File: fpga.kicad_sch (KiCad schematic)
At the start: 2 parts, among them Y1 CXO_DIP14

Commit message: add notes
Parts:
- added C10, C11, C12, C13, C14, C15, C16, C17, C18, C19, C20, C21: 0.1uF, Capacitor_SMD:C_0603_1608Metric, symbol Device:C_Small
- added R10, R11, R12, R13, R14, R15, R16, R17, R18, R19, R20, R21, R22, R23, R24, R25, R26, R27, R28, R29, R30, R31, R32, R33, R34, R7, R8, R9: 220R, Resistor_SMD:R_0603_1608Metric, symbol Device:R_Small
- added U3, U4, U7: TXU0104PWR, Library:TSSOP_0104PWR, symbol Library:TXU0104PWR
- added U5, U6, U8: TXB0104PWR, Library:TSSOP_0104PWR, symbol Library:TXB0104PWR
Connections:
- net +3.3V: now also Y1.1 (EN), Y1.14 (Vcc), C15.1, C16.1, C17.1, C18.1, C19.1, C20.1, U3.1 (VCCA), U4.1 (VCCA), U5.1 (VCCA), U6.1 (VCCA), U7.1 (VCCA), U8.7 (GND)
- net +5V: now also C10.1, C11.1, C12.1, C13.1, C14.1, C21.1, U3.14 (VCCB), U3.8 (OE), U4.14 (VCCB), U4.8 (OE), U5.14 (VCCB), U5.8 (OE), U6.14 (VCCB), U6.8 (OE), U7.14 (VCCB), U7.8 (OE), U8.14 (VCCB), U8.8 (OE); no longer Y1.1 (EN), Y1.14 (Vcc)
- net GND: now also C10.2, C11.2, C12.2, C13.2, C14.2, C15.2, C16.2, C17.2, C18.2, C19.2, C20.2, C21.2, U3.7 (GND), U4.7 (GND), U5.7 (GND), U6.7 (GND), U7.7 (GND), U8.1 (VCCA)
- net DL5: now reaches U2.10 (R7)
- net at U2.11 (R6): now also U7.3 (A2)
- net DL4: now reaches U2.12 (T5)
- net at U2.13 (R5): now also U7.2 (A1)
- net DL3: now reaches U2.14 (T4)
- net Z0: now reaches U2.15 (U6)
- net DL2: now reaches U2.16 (U5)
- net Z1: now reaches U2.17 (V4)
- net DL1: now reaches U2.18 (U4)
- net Z2: now reaches U2.19 (V3)
- net DL0: now reaches U2.20 (V2)
- net Z3: now reaches U2.21 (U2)
- net at U2.22 (U1): now also U4.3 (A2)
- net Z4: now reaches U2.23 (P4)
- net at U2.24 (T3): now also U4.4 (A3)
- net Z5: now reaches U2.25 (R3)
- net at U2.26 (T2): now also U4.5 (A4)
- net Z6: now reaches U2.27 (N4)
- net at U2.28 (P3): now also R7.1
- net Z7: now reaches U2.29 (M6)
- net at U2.30 (M5): now also R16.1
- net Z8: now reaches U2.31 (L5)
- net at U2.32 (L4): now also R15.1
- net Z9: now reaches U2.33 (K3)
- net at U2.34 (K5): now also R14.1
- net Z10: now reaches U2.35 (P1)
- net at U2.36 (R1): now also R8.1
- net Z11: now reaches U2.37 (N1)
- net at U2.38 (N2): now also R9.1
- net Z12: now reaches U2.39 (M2)
- net at U2.40 (M1): now also R10.1
- net Z13: now reaches U2.41 (J5)
- net at U2.42 (J4): now also R11.1
- net Z14: now reaches U2.43 (J6)
- net at U2.44 (K6): now also R12.1
- net Z15: now reaches U2.45 (L2)
- net at U2.46 (L3): now also R13.1
- net Z16: now reaches U2.47 (K2)
- net at U2.48 (K1): now also R34.1
- net at U2.5 (V8): now also U4.2 (A1)
- net DL7: now reaches U2.6 (V7)
- net at U2.7 (U7): now also U7.5 (A4)
- net DL6: now reaches U2.8 (V6)
- net at U2.9 (T7): now also U7.4 (A3)
- net at U2.55 (F18): now also U6.5 (A4)
- net at U2.56 (G17): now also U6.4 (A3)
- net at U2.57 (E18): now also U6.3 (A2)
- net at U2.58 (F17): now also U6.2 (A1)
- net at U2.59 (D18): now also U5.2 (A1)
- net at U2.60 (E17): now also U5.3 (A2)
- net at U2.61 (C17): now also U5.4 (A3)
- net at U2.62 (C18): now also U5.5 (A4)
- net at U2.63 (G15): now also R17.1
- net at U2.65 (F15): now also R18.1
- net at U2.67 (E16): now also R19.1
- net at U2.68 (E15): now also U3.2 (A1)
- net at U2.69 (D16): now also R20.1
- net at U2.70 (D15): now also U3.3 (A2)
- net at U2.71 (A17): now also R21.1
- net at U2.72 (B17): now also U3.4 (A3)
- net at U2.73 (C16): now also R22.1
- net at U2.74 (B16): now also U3.5 (A4)
- net at U2.75 (A15): now also R23.1
- net Z21: now reaches U2.76 (B15)
- net at U2.77 (A14): now also R24.1
- net Z20: now reaches U2.78 (B14)
- net at U2.79 (C14): now also R25.1
- net Z19: now reaches U2.80 (D14)
- net at U2.81 (C13): now also R26.1
- net Z18: now reaches U2.82 (D13)
- net at U2.83 (A13): now also R27.1
- net Z17: now reaches U2.84 (C12)
- net at U2.85 (F14): now also R28.1
- net at U2.86 (E13): now also R33.1
- net at U2.87 (B12): now also R29.1
- net at U2.88 (A12): now also U8.2 (A1)
- net at U2.89 (C11): now also R30.1
- net at U2.90 (B11): now also U8.3 (A2)
- net at U2.91 (D11): now also R31.1
- net at U2.93 (C9): now also R32.1
- new net A0: R17.2
- new net A1: R18.2
- new net A10: R27.2
- new net A11: R28.2
- new net A12: R29.2
- new net A13: R30.2
- new net A14: R31.2
- new net A15: R32.2
- new net A2: R19.2
- new net A3: R20.2
- new net A4: R21.2
- new net A5: R22.2
- new net A6: R23.2
- new net A7: R24.2
- new net A8: R25.2
- new net A9: R26.2
- new net AVMA: R15.2
- new net BA: R11.2
- new net BS: R13.2
- new net CPU_BUSY: R16.2
- new net D0: U5.10 (B4)
- new net D1: U5.11 (B3)
- new net D2: U5.12 (B2)
- new net D3: U5.13 (B1)
- new net D4: U6.10 (B4)
- new net D5: U6.11 (B3)
- new net D6: U6.12 (B2)
- new net D7: U6.13 (B1)
- new net E: U3.13 (B1Y)
- new net EXTMEN: R33.2
- new net LIC: R9.2
- new net Q: U3.12 (B2Y)
- new net R0: U8.12 (B2)
- new net R1: U8.13 (B1)
- new net R/~{W}: R34.2
- new net S0: U4.13 (B1Y)
- new net S1: U7.10 (B4Y)
- new net S2: U7.11 (B3Y)
- new net S3: U7.12 (B2Y)
- new net S4: U7.13 (B1Y)
- new net TSC: R14.2
- new net VCLK: U3.10 (B4Y)
- new net ~{FIRQ}: U4.11 (B3Y)
- new net ~{FIRQ}p: R10.2
- new net ~{HALT}: U3.11 (B3Y)
- new net ~{IRQ}: U4.12 (B2Y)
- new net ~{IRQ}p: R8.2
- new net ~{NMI}: U4.10 (B4Y)
- new net ~{NMI}p: R12.2
- new net ~{RESET}: R7.2
- no-connect marks 0 -> 24
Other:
- note added: "Crystal footprint needs to meet DIP14 and DIP8 specs"
- moved on the sheet: U2A, U2B, Y1

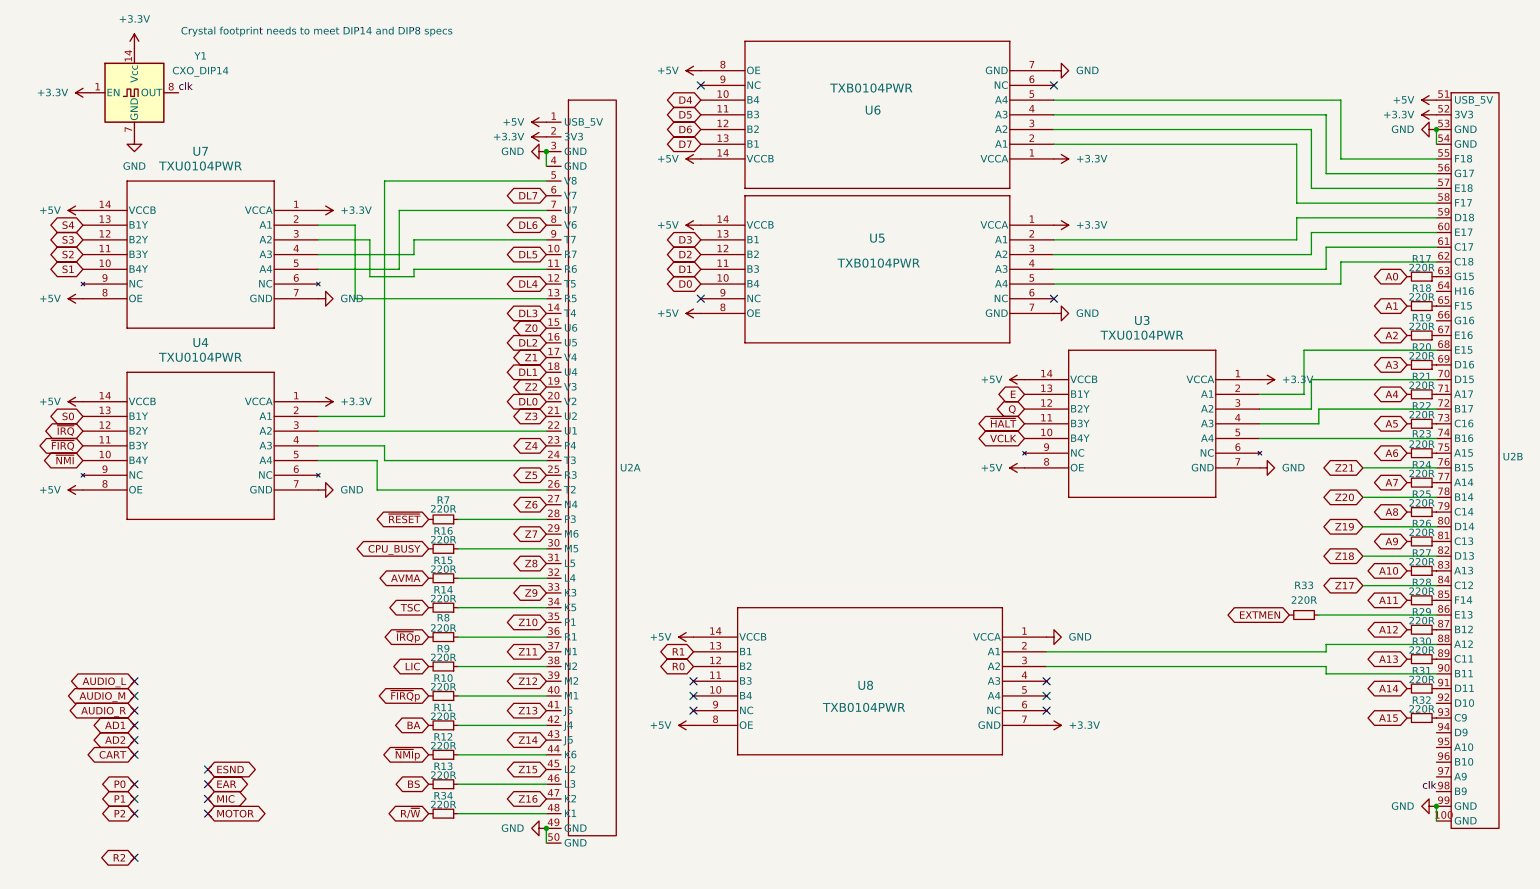
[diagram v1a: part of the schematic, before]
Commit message: revise bus tracing
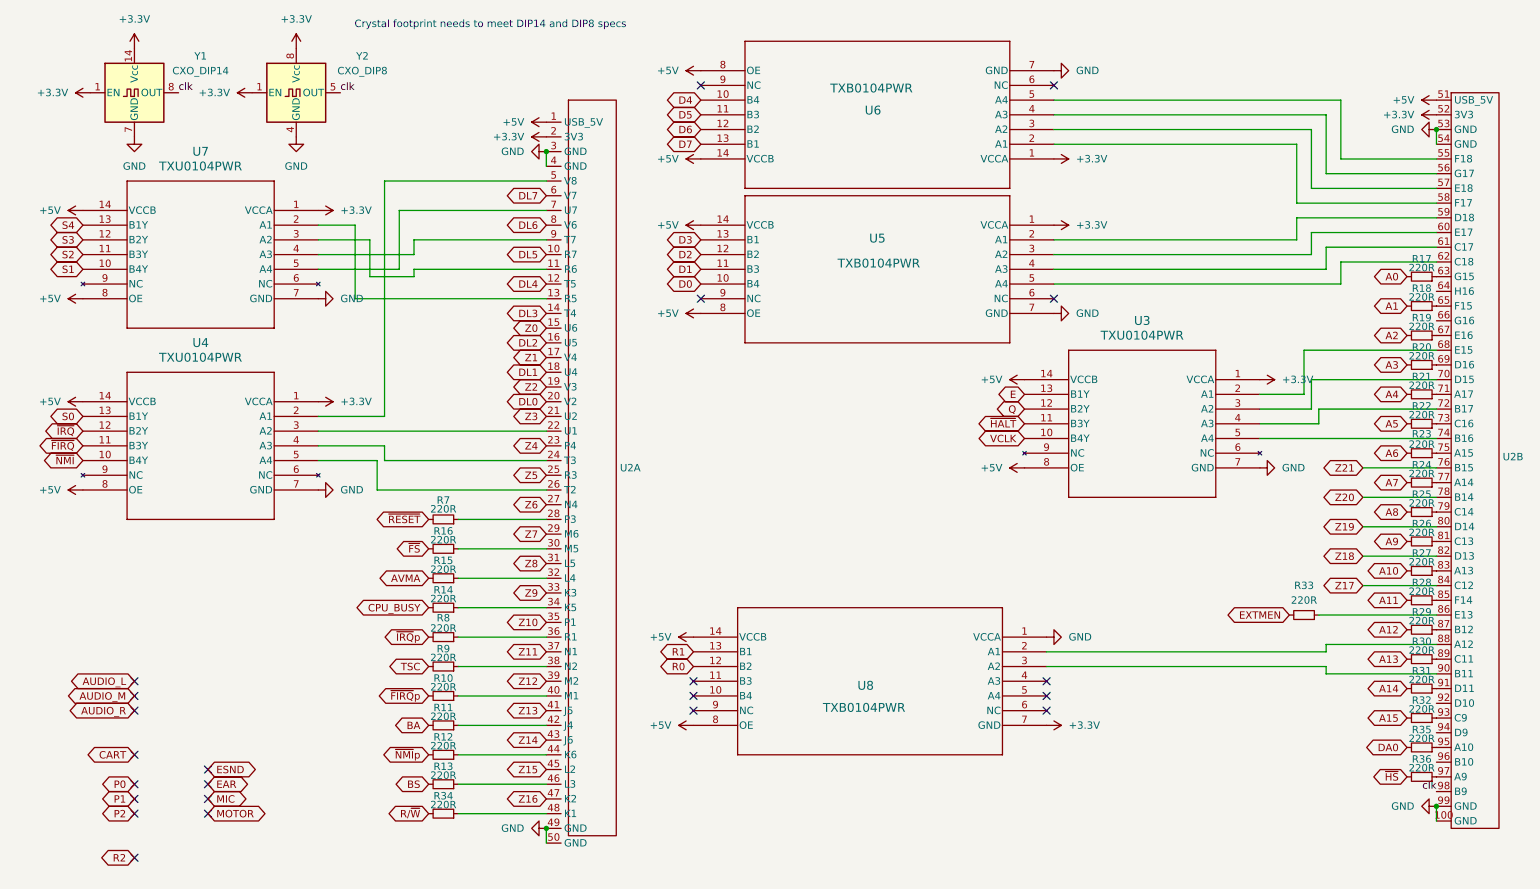
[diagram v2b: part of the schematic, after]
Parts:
- added R35, R36: 220R, Resistor_SMD:R_0603_1608Metric, symbol Device:R_Small
- added Y2: CXO_DIP8, Oscillator:Oscillator_DIP-8, symbol Oscillator:CXO_DIP8
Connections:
- net LIC is gone; now on net TSC: R9.2
- net +3.3V: now also Y2.1 (EN), Y2.8 (Vcc)
- net CPU_BUSY: now also R14.2; no longer R16.2
- net GND: now also Y2.4 (GND)
- net TSC: no longer R14.2
- net clk: now also Y2.5 (OUT)
- net at U2.95 (A10): now also R35.1
- net at U2.97 (A9): now also R36.1
- new net DA0: R35.2
- new net ~{FS}: R16.2
- new net ~{HS}: R36.2
- no-connect marks 24 -> 22

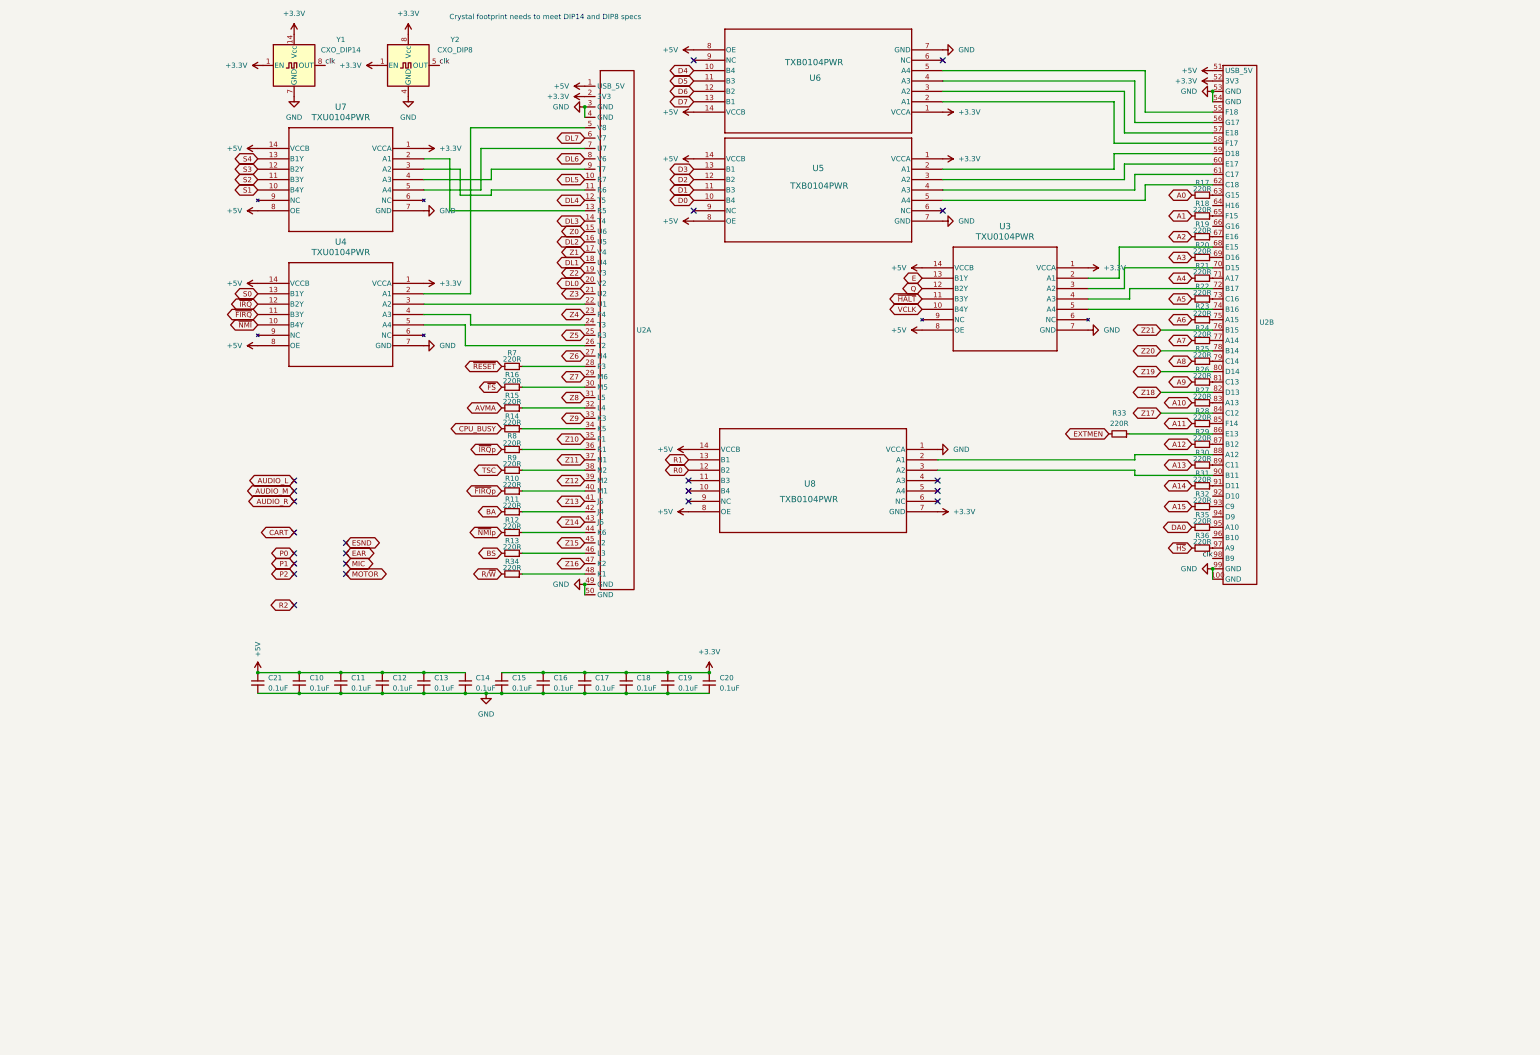
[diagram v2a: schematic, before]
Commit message: reinforce level shifting
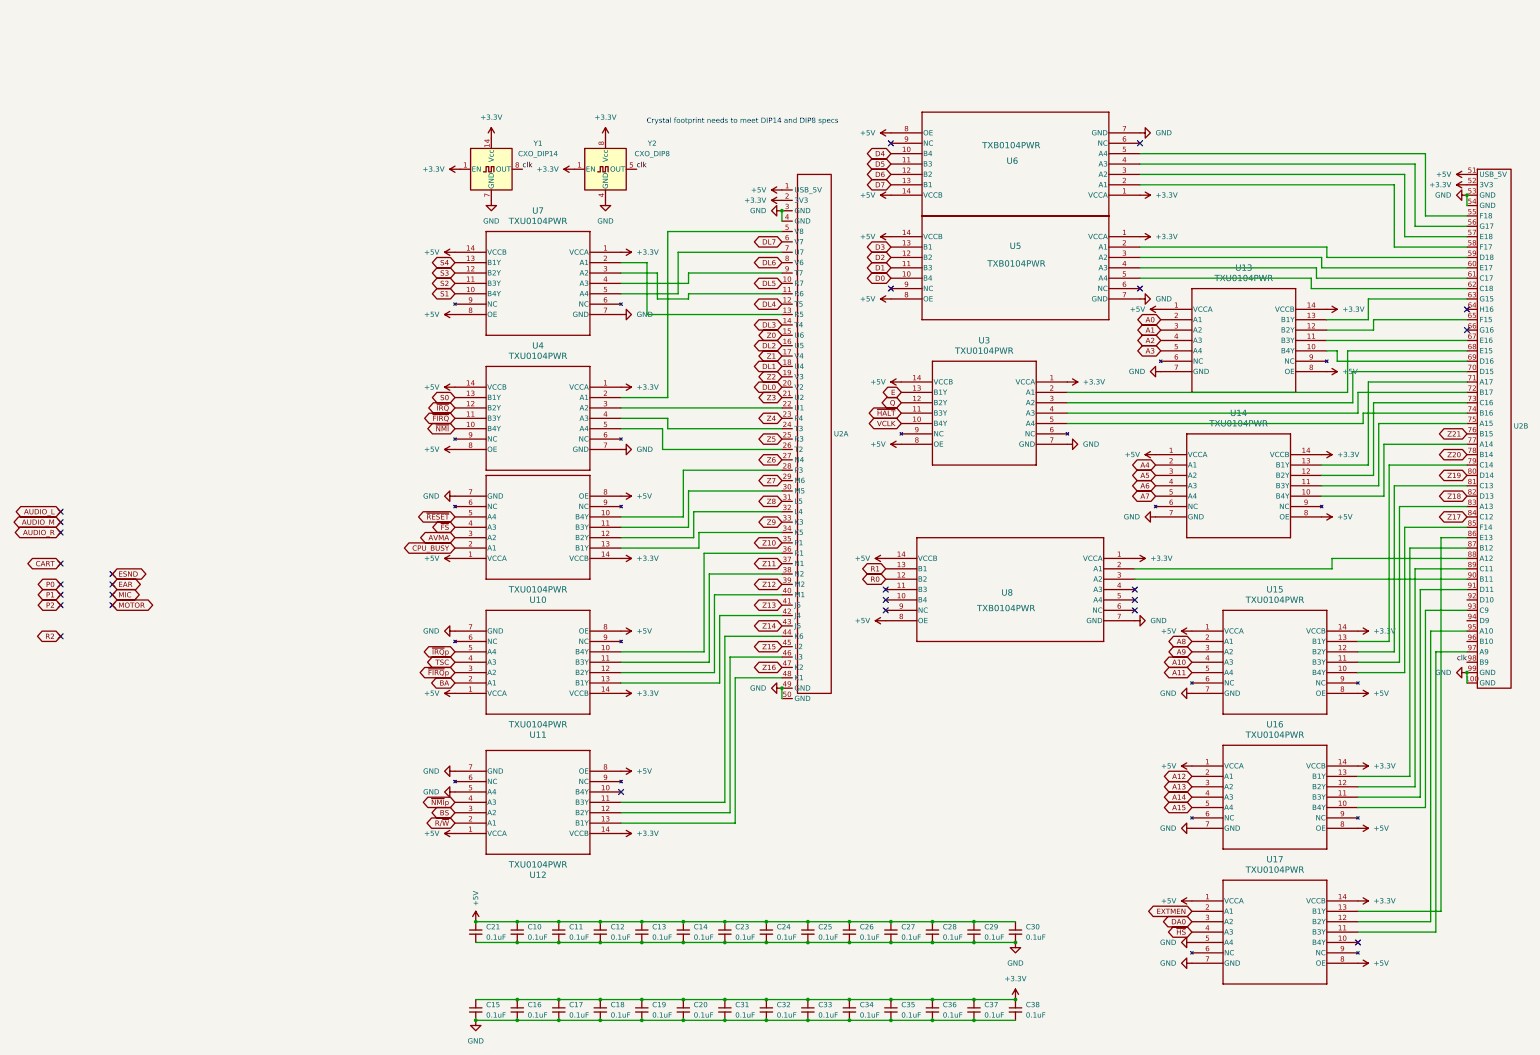
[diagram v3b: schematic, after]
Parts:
- removed R10, R11, R12, R13, R14, R15, R16, R17, R18, R19, R20, R21, R22, R23, R24, R25, R26, R27, R28, R29, R30, R31, R32, R33, R34, R35, R36, R7, R8, R9: 220R, Resistor_SMD:R_0603_1608Metric, symbol Device:R_Small
- added C23, C24, C25, C26, C27, C28, C29, C30, C31, C32, C33, C34, C35, C36, C37, C38: 0.1uF, Capacitor_SMD:C_0603_1608Metric, symbol Device:C_Small
- added U10, U11, U12, U13, U14, U15, U16, U17: TXU0104PWR, Library:TSSOP_0104PWR, symbol Library:TXU0104PWR
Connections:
- net +3.3V: now also U8.1 (VCCA), C31.1, C32.1, C33.1, C34.1, C35.1, C36.1, C37.1, C38.1, U10.14 (VCCB), U11.14 (VCCB), U12.14 (VCCB), U13.14 (VCCB), U14.14 (VCCB), U15.14 (VCCB), U16.14 (VCCB), U17.14 (VCCB); no longer U8.7 (GND)
- net +5V: now also C23.1, C24.1, C25.1, C26.1, C27.1, C28.1, C29.1, C30.1, U10.1 (VCCA), U10.8 (OE), U11.1 (VCCA), U11.8 (OE), U12.1 (VCCA), U12.8 (OE), U13.1 (VCCA), U13.8 (OE), U14.1 (VCCA), U14.8 (OE), U15.1 (VCCA), U15.8 (OE), U16.1 (VCCA), U16.8 (OE), U17.1 (VCCA), U17.8 (OE)
- net A0: now also U13.2 (A1)
- net A1: now also U13.3 (A2)
- net A10: now also U15.4 (A3)
- net A11: now also U15.5 (A4)
- net A12: now also U16.2 (A1)
- net A13: now also U16.3 (A2)
- net A14: now also U16.4 (A3)
- net A15: now also U16.5 (A4)
- net A2: now also U13.4 (A3)
- net A3: now also U13.5 (A4)
- net A4: now also U14.2 (A1)
- net A5: now also U14.3 (A2)
- net A6: now also U14.4 (A3)
- net A7: now also U14.5 (A4)
- net A8: now also U15.2 (A1)
- net A9: now also U15.3 (A2)
- net AVMA: now also U10.3 (A2)
- net BA: now also U11.2 (A1)
- net BS: now also U12.3 (A2)
- net CPU_BUSY: now also U10.2 (A1)
- net DA0: now also U17.3 (A2)
- net EXTMEN: now also U17.2 (A1)
- net GND: now also U8.7 (GND), C23.2, C24.2, C25.2, C26.2, C27.2, C28.2, C29.2, C30.2, C31.2, C32.2, C33.2, C34.2, C35.2, C36.2, C37.2, C38.2, U10.7 (GND), U11.7 (GND), U12.5 (A4), U12.7 (GND), U13.7 (GND), U14.7 (GND), U15.7 (GND), U16.7 (GND), U17.5 (A4), U17.7 (GND); no longer U8.1 (VCCA)
- net R/~{W}: now also U12.2 (A1)
- net TSC: now also U11.4 (A3)
- net ~{FIRQ}p: now also U11.3 (A2)
- net ~{FS}: now also U10.4 (A3)
- net ~{HS}: now also U17.4 (A3)
- net ~{IRQ}p: now also U11.5 (A4)
- net ~{NMI}p: now also U12.4 (A3)
- net ~{RESET}: now also U10.5 (A4)
- net at U2.77 (A14): now also U14.10 (B4Y)
- net at U2.38 (N2): now also U11.11 (B3Y)
- net at U2.81 (C13): now also U15.12 (B2Y)
- net at U2.95 (A10): now also U17.12 (B2Y)
- net at U2.48 (K1): now also U12.13 (B1Y)
- net at U2.28 (P3): now also U10.10 (B4Y)
- net at U2.30 (M5): now also U10.11 (B3Y)
- net at U2.32 (L4): now also U10.12 (B2Y)
- net at U2.34 (K5): now also U10.13 (B1Y)
- net at U2.36 (R1): now also U11.10 (B4Y)
- net at U2.40 (M1): now also U11.12 (B2Y)
- net at U2.42 (J4): now also U11.13 (B1Y)
- net at U2.44 (K6): now also U12.11 (B3Y)
- net at U2.46 (L3): now also U12.12 (B2Y)
- net at U2.89 (C11): now also U16.12 (B2Y)
- net at U2.71 (A17): now also U14.13 (B1Y)
- net at U2.87 (B12): now also U16.13 (B1Y)
- net at U2.79 (C14): now also U15.13 (B1Y)
- net at U2.63 (G15): now also U13.13 (B1Y)
- net at U2.65 (F15): now also U13.12 (B2Y)
- net at U2.67 (E16): now also U13.11 (B3Y)
- net at U2.69 (D16): now also U13.10 (B4Y)
- net at U2.73 (C16): now also U14.12 (B2Y)
- net at U2.75 (A15): now also U14.11 (B3Y)
- net at U2.83 (A13): now also U15.11 (B3Y)
- net at U2.85 (F14): now also U15.10 (B4Y)
- net at U2.86 (E13): now also U17.13 (B1Y)
- net at U2.91 (D11): now also U16.11 (B3Y)
- net at U2.93 (C9): now also U16.10 (B4Y)
- net at U2.97 (A9): now also U17.11 (B3Y)
- no-connect marks 22 -> 26
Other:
- moved on the sheet: C10, C11, C12, C13, C14, C15, C16, C17, C18, C19, C20, C21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
